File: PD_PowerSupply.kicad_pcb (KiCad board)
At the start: 2 copper layers, 10 parts, among them J1 USB4085-GF-A_REVA, Q1 STL6P3LLH6, Q2 STL6P3LLH6, U1 STUSB4500QTR, U2 ESP32-WROOM-32, U3 CP2102N, U4 IR38062MTRPBF, U5 IR38062MTRPBF, U6 LTC3886

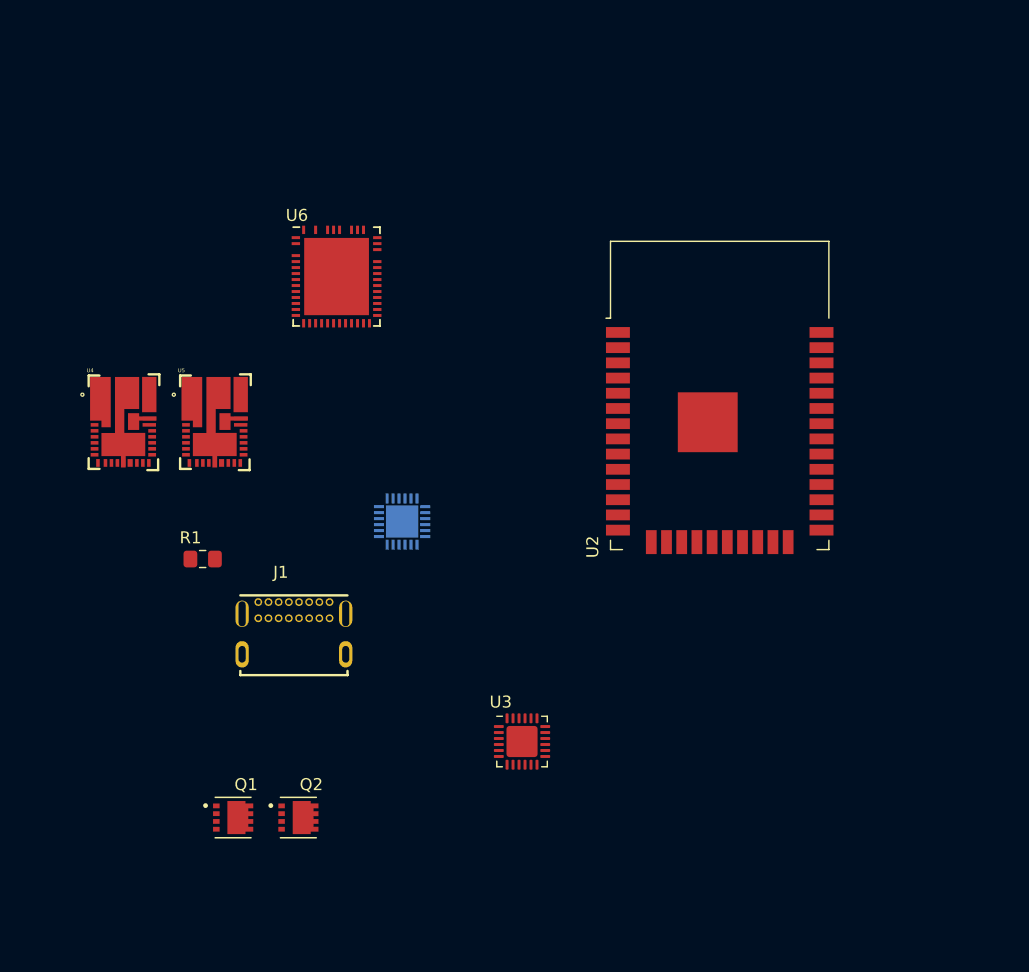
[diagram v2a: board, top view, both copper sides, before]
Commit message: added footprints and symbol for LTC2972
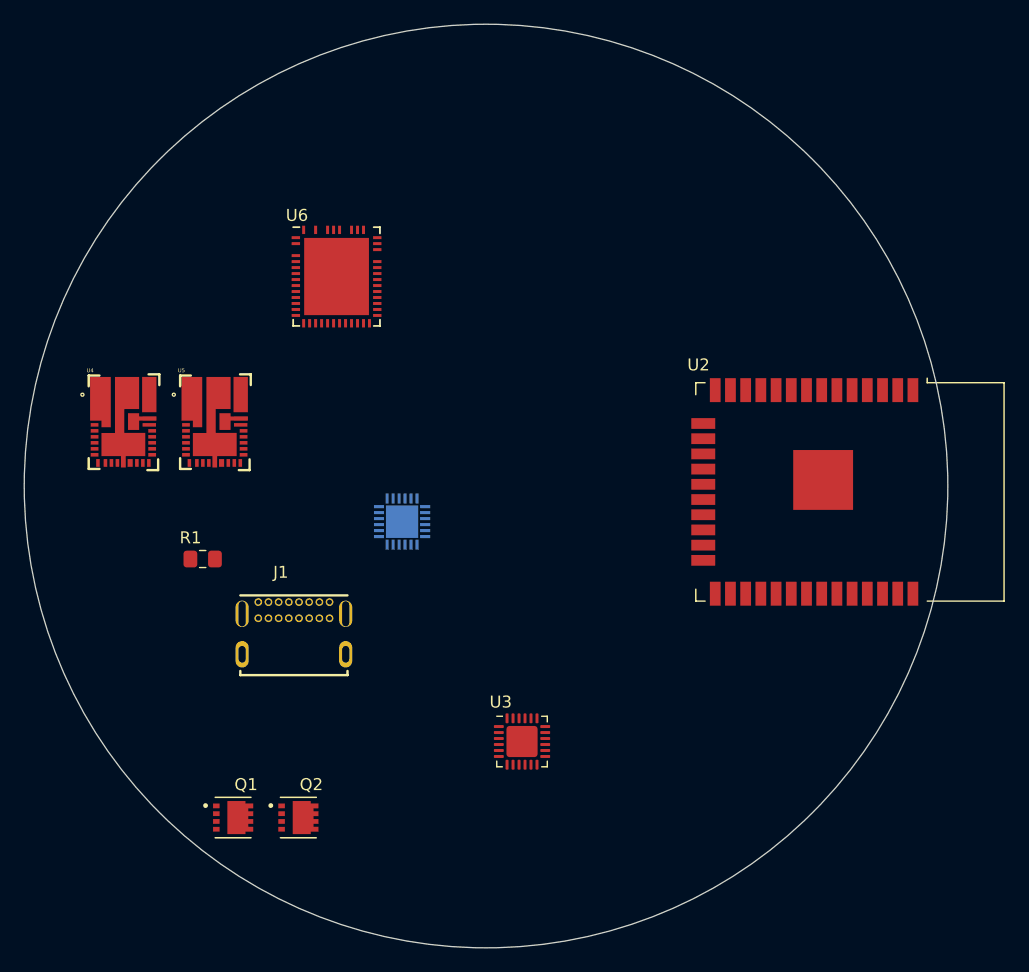
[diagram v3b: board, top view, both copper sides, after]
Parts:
- moved U2 9.37 mm to (110.8, 102.3), turned to 270 degrees
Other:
- board outline added: 77.1 x 77.1 mm
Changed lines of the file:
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@@
   (general
     (thickness 1.6)
-    (drawings 0)
+    (drawings 1)
     (tracks 0)
     (zones 0)
@@
   )
   (module RF_Module:ESP32-WROOM-32 (layer F.Cu)
-    (at 102.87 97.282)
+    (at 110.751 102.346 270)
     (descr "Single 2.4 GHz Wi-Fi and Bluetooth combo chip https://www.espressif.com/sites/default/files/documentation/esp32-wroom-32_datasheet_en.pdf")
     (tags "Single 2.4 GHz Wi-Fi and Bluetooth combo  chip")
     (attr smd)
-    (fp_text reference U2 (at -10.61 9.652 90) (layer F.SilkS)
+    (fp_text reference U2 (at -10.61 9.652) (layer F.SilkS)
       (effects (font (size 1 1) (thickness 0.15)))
     )
-    (fp_text value ESP32-WROOM-32 (at 0 11.5) (layer F.Fab)
+    (fp_text value ESP32-WROOM-32 (at 0 11.5 90) (layer F.Fab)
       (effects (font (size 1 1) (thickness 0.15)))
     )
@@
     (fp_line (start 9 9.76) (end 9 -15.745) (layer F.Fab) (width 0.1))
     (fp_line (start -14 -9.97) (end -14 -20.75) (layer Dwgs.User) (width 0.1))
-    (fp_text user "5 mm" (at 7.8 -19.075 90) (layer Cmts.User)
+    (fp_text user "5 mm" (at 7.8 -19.075) (layer Cmts.User)
       (effects (font (size 0.5 0.5) (thickness 0.1)))
     )
-    (fp_text user "5 mm" (at -11.2 -14.375) (layer Cmts.User)
+    (fp_text user "5 mm" (at -11.2 -14.375 90) (layer Cmts.User)
       (effects (font (size 0.5 0.5) (thickness 0.1)))
     )
-    (fp_text user "5 mm" (at 11.8 -14.375) (layer Cmts.User)
+    (fp_text user "5 mm" (at 11.8 -14.375 90) (layer Cmts.User)
       (effects (font (size 0.5 0.5) (thickness 0.1)))
     )
-    (fp_text user Antenna (at 0 -13) (layer Cmts.User)
+    (fp_text user Antenna (at 0 -13 90) (layer Cmts.User)
       (effects (font (size 1 1) (thickness 0.15)))
     )
-    (fp_text user "KEEP-OUT ZONE" (at 0 -19) (layer Cmts.User)
+    (fp_text user "KEEP-OUT ZONE" (at 0 -19 90) (layer Cmts.User)
       (effects (font (size 1 1) (thickness 0.15)))
     )
-    (fp_text user %R (at 0 0) (layer F.Fab)
+    (fp_text user %R (at 0 0 90) (layer F.Fab)
       (effects (font (size 1 1) (thickness 0.15)))
     )
-    (pad 38 smd rect (at 8.5 -8.255) (size 2 0.9) (layers F.Cu F.Paste F.Mask)
-      (net 42 GND))
-    (pad 37 smd rect (at 8.5 -6.985) (size 2 0.9) (layers F.Cu F.Paste F.Mask)
+    (pad 38 smd rect (at 8.5 -8.255 270) (size 2 0.9) (layers F.Cu F.Paste F.Mask)
+      (net 42 GND))
+    (pad 37 smd rect (at 8.5 -6.985 270) (size 2 0.9) (layers F.Cu F.Paste F.Mask)
       (net 1 "Net-(U2-Pad37)"))
-    (pad 36 smd rect (at 8.5 -5.715) (size 2 0.9) (layers F.Cu F.Paste F.Mask)
+    (pad 36 smd rect (at 8.5 -5.715 270) (size 2 0.9) (layers F.Cu F.Paste F.Mask)
       (net 2 /I2C_SCL))
-    (pad 35 smd rect (at 8.5 -4.445) (size 2 0.9) (layers F.Cu F.Paste F.Mask)
+    (pad 35 smd rect (at 8.5 -4.445 270) (size 2 0.9) (layers F.Cu F.Paste F.Mask)
       (net 3 "Net-(U2-Pad35)"))
-    (pad 34 smd rect (at 8.5 -3.175) (size 2 0.9) (layers F.Cu F.Paste F.Mask)
+    (pad 34 smd rect (at 8.5 -3.175 270) (size 2 0.9) (layers F.Cu F.Paste F.Mask)
       (net 4 "Net-(U2-Pad34)"))
-    (pad 33 smd rect (at 8.5 -1.905) (size 2 0.9) (layers F.Cu F.Paste F.Mask)
+    (pad 33 smd rect (at 8.5 -1.905 270) (size 2 0.9) (layers F.Cu F.Paste F.Mask)
       (net 5 /I2C_SDA))
-    (pad 32 smd rect (at 8.5 -0.635) (size 2 0.9) (layers F.Cu F.Paste F.Mask)
+    (pad 32 smd rect (at 8.5 -0.635 270) (size 2 0.9) (layers F.Cu F.Paste F.Mask)
       (net 6 "Net-(U2-Pad32)"))
-    (pad 31 smd rect (at 8.5 0.635) (size 2 0.9) (layers F.Cu F.Paste F.Mask)
+    (pad 31 smd rect (at 8.5 0.635 270) (size 2 0.9) (layers F.Cu F.Paste F.Mask)
       (net 7 "Net-(U2-Pad31)"))
-    (pad 30 smd rect (at 8.5 1.905) (size 2 0.9) (layers F.Cu F.Paste F.Mask)
+    (pad 30 smd rect (at 8.5 1.905 270) (size 2 0.9) (layers F.Cu F.Paste F.Mask)
       (net 8 "Net-(U2-Pad30)"))
-    (pad 29 smd rect (at 8.5 3.175) (size 2 0.9) (layers F.Cu F.Paste F.Mask)
+    (pad 29 smd rect (at 8.5 3.175 270) (size 2 0.9) (layers F.Cu F.Paste F.Mask)
       (net 9 "Net-(U2-Pad29)"))
-    (pad 28 smd rect (at 8.5 4.445) (size 2 0.9) (layers F.Cu F.Paste F.Mask)
+    (pad 28 smd rect (at 8.5 4.445 270) (size 2 0.9) (layers F.Cu F.Paste F.Mask)
       (net 10 "Net-(U2-Pad28)"))
-    (pad 27 smd rect (at 8.5 5.715) (size 2 0.9) (layers F.Cu F.Paste F.Mask)
+    (pad 27 smd rect (at 8.5 5.715 270) (size 2 0.9) (layers F.Cu F.Paste F.Mask)
       (net 11 "Net-(U2-Pad27)"))
-    (pad 26 smd rect (at 8.5 6.985) (size 2 0.9) (layers F.Cu F.Paste F.Mask)
+    (pad 26 smd rect (at 8.5 6.985 270) (size 2 0.9) (layers F.Cu F.Paste F.Mask)
       (net 12 "Net-(U2-Pad26)"))
-    (pad 25 smd rect (at 8.5 8.255) (size 2 0.9) (layers F.Cu F.Paste F.Mask)
+    (pad 25 smd rect (at 8.5 8.255 270) (size 2 0.9) (layers F.Cu F.Paste F.Mask)
       (net 13 "Net-(U2-Pad25)"))
-    (pad 24 smd rect (at 5.715 9.255 90) (size 2 0.9) (layers F.Cu F.Paste F.Mask)
+    (pad 24 smd rect (at 5.715 9.255) (size 2 0.9) (layers F.Cu F.Paste F.Mask)
       (net 14 "Net-(U2-Pad24)"))
-    (pad 23 smd rect (at 4.445 9.255 90) (size 2 0.9) (layers F.Cu F.Paste F.Mask)
+    (pad 23 smd rect (at 4.445 9.255) (size 2 0.9) (layers F.Cu F.Paste F.Mask)
       (net 15 "Net-(U2-Pad23)"))
-    (pad 22 smd rect (at 3.175 9.255 90) (size 2 0.9) (layers F.Cu F.Paste F.Mask)
+    (pad 22 smd rect (at 3.175 9.255) (size 2 0.9) (layers F.Cu F.Paste F.Mask)
       (net 16 "Net-(U2-Pad22)"))
-    (pad 21 smd rect (at 1.905 9.255 90) (size 2 0.9) (layers F.Cu F.Paste F.Mask)
+    (pad 21 smd rect (at 1.905 9.255) (size 2 0.9) (layers F.Cu F.Paste F.Mask)
       (net 17 "Net-(U2-Pad21)"))
-    (pad 20 smd rect (at 0.635 9.255 90) (size 2 0.9) (layers F.Cu F.Paste F.Mask)
+    (pad 20 smd rect (at 0.635 9.255) (size 2 0.9) (layers F.Cu F.Paste F.Mask)
       (net 18 "Net-(U2-Pad20)"))
-    (pad 19 smd rect (at -0.635 9.255 90) (size 2 0.9) (layers F.Cu F.Paste F.Mask)
+    (pad 19 smd rect (at -0.635 9.255) (size 2 0.9) (layers F.Cu F.Paste F.Mask)
       (net 19 "Net-(U2-Pad19)"))
-    (pad 18 smd rect (at -1.905 9.255 90) (size 2 0.9) (layers F.Cu F.Paste F.Mask)
+    (pad 18 smd rect (at -1.905 9.255) (size 2 0.9) (layers F.Cu F.Paste F.Mask)
       (net 20 "Net-(U2-Pad18)"))
-    (pad 17 smd rect (at -3.175 9.255 90) (size 2 0.9) (layers F.Cu F.Paste F.Mask)
+    (pad 17 smd rect (at -3.175 9.255) (size 2 0.9) (layers F.Cu F.Paste F.Mask)
       (net 21 "Net-(U2-Pad17)"))
-    (pad 16 smd rect (at -4.445 9.255 90) (size 2 0.9) (layers F.Cu F.Paste F.Mask)
+    (pad 16 smd rect (at -4.445 9.255) (size 2 0.9) (layers F.Cu F.Paste F.Mask)
       (net 22 "Net-(U2-Pad16)"))
-    (pad 15 smd rect (at -5.715 9.255 90) (size 2 0.9) (layers F.Cu F.Paste F.Mask)
-      (net 42 GND))
-    (pad 14 smd rect (at -8.5 8.255) (size 2 0.9) (layers F.Cu F.Paste F.Mask)
+    (pad 15 smd rect (at -5.715 9.255) (size 2 0.9) (layers F.Cu F.Paste F.Mask)
+      (net 42 GND))
+    (pad 14 smd rect (at -8.5 8.255 270) (size 2 0.9) (layers F.Cu F.Paste F.Mask)
       (net 23 "Net-(U2-Pad14)"))
-    (pad 13 smd rect (at -8.5 6.985) (size 2 0.9) (layers F.Cu F.Paste F.Mask)
+    (pad 13 smd rect (at -8.5 6.985 270) (size 2 0.9) (layers F.Cu F.Paste F.Mask)
       (net 24 "Net-(U2-Pad13)"))
-    (pad 12 smd rect (at -8.5 5.715) (size 2 0.9) (layers F.Cu F.Paste F.Mask)
+    (pad 12 smd rect (at -8.5 5.715 270) (size 2 0.9) (layers F.Cu F.Paste F.Mask)
       (net 25 "Net-(U2-Pad12)"))
-    (pad 11 smd rect (at -8.5 4.445) (size 2 0.9) (layers F.Cu F.Paste F.Mask)
+    (pad 11 smd rect (at -8.5 4.445 270) (size 2 0.9) (layers F.Cu F.Paste F.Mask)
       (net 26 "Net-(U2-Pad11)"))
-    (pad 10 smd rect (at -8.5 3.175) (size 2 0.9) (layers F.Cu F.Paste F.Mask)
+    (pad 10 smd rect (at -8.5 3.175 270) (size 2 0.9) (layers F.Cu F.Paste F.Mask)
       (net 27 "Net-(U2-Pad10)"))
-    (pad 9 smd rect (at -8.5 1.905) (size 2 0.9) (layers F.Cu F.Paste F.Mask)
+    (pad 9 smd rect (at -8.5 1.905 270) (size 2 0.9) (layers F.Cu F.Paste F.Mask)
       (net 28 "Net-(U2-Pad9)"))
-    (pad 8 smd rect (at -8.5 0.635) (size 2 0.9) (layers F.Cu F.Paste F.Mask)
+    (pad 8 smd rect (at -8.5 0.635 270) (size 2 0.9) (layers F.Cu F.Paste F.Mask)
       (net 29 "Net-(U2-Pad8)"))
-    (pad 7 smd rect (at -8.5 -0.635) (size 2 0.9) (layers F.Cu F.Paste F.Mask)
+    (pad 7 smd rect (at -8.5 -0.635 270) (size 2 0.9) (layers F.Cu F.Paste F.Mask)
       (net 53 /STUSB_ALERT))
-    (pad 6 smd rect (at -8.5 -1.905) (size 2 0.9) (layers F.Cu F.Paste F.Mask)
+    (pad 6 smd rect (at -8.5 -1.905 270) (size 2 0.9) (layers F.Cu F.Paste F.Mask)
       (net 50 /STUSB_RESET))
-    (pad 5 smd rect (at -8.5 -3.175) (size 2 0.9) (layers F.Cu F.Paste F.Mask)
+    (pad 5 smd rect (at -8.5 -3.175 270) (size 2 0.9) (layers F.Cu F.Paste F.Mask)
       (net 30 "Net-(U2-Pad5)"))
-    (pad 4 smd rect (at -8.5 -4.445) (size 2 0.9) (layers F.Cu F.Paste F.Mask)
+    (pad 4 smd rect (at -8.5 -4.445 270) (size 2 0.9) (layers F.Cu F.Paste F.Mask)
       (net 31 "Net-(U2-Pad4)"))
-    (pad 3 smd rect (at -8.5 -5.715) (size 2 0.9) (layers F.Cu F.Paste F.Mask)
+    (pad 3 smd rect (at -8.5 -5.715 270) (size 2 0.9) (layers F.Cu F.Paste F.Mask)
       (net 32 "Net-(U2-Pad3)"))
-    (pad 2 smd rect (at -8.5 -6.985) (size 2 0.9) (layers F.Cu F.Paste F.Mask)
+    (pad 2 smd rect (at -8.5 -6.985 270) (size 2 0.9) (layers F.Cu F.Paste F.Mask)
       (net 59 +3V3))
-    (pad 1 smd rect (at -8.5 -8.255) (size 2 0.9) (layers F.Cu F.Paste F.Mask)
-      (net 42 GND))
-    (pad 39 smd rect (at -1 -0.755) (size 5 5) (layers F.Cu F.Paste F.Mask)
+    (pad 1 smd rect (at -8.5 -8.255 270) (size 2 0.9) (layers F.Cu F.Paste F.Mask)
+      (net 42 GND))
+    (pad 39 smd rect (at -1 -0.755 270) (size 5 5) (layers F.Cu F.Paste F.Mask)
       (net 42 GND))
     (model ${KISYS3DMOD}/RF_Module.3dshapes/ESP32-WROOM-32.wrl
@@
     )
   )
+  (gr_circle (center 83.354636 101.854) (end 120.692636 111.506) (layer Edge.Cuts) (width 0.05))
 )

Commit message: set up coprocessor
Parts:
- added Q3: MMBT3906, Package_TO_SOT_SMD:SOT-23, F.Cu at (94.1, 132.8)
- added Q4: MMBT3906, Package_TO_SOT_SMD:SOT-23, F.Cu at (98.5, 132.8)
- U4, U5: value IR38062MTRPBF -> LTM8074IY#PBF; footprint IR38062MTRPBF:PQFN50P700X500X100-26N -> LTM8074IY_PBF:BGA25C65P5X5_400X400X198N
- U6: value LTC3886 -> LTC2972; footprint Package_DFN_QFN:Linear_UGK52_QFN-46-52 -> LTC2972:LTC2972
- moved U4 53.1 mm to (98.4, 124.1)
- moved U5 52.6 mm to (107.2, 121.2)
- moved U6 37.3 mm to (94.0, 113.6)
- renumbered J1 to USB1
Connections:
- Q1 pad 5_6_7_8: VBUS -> Net-(D1-Pad2)
- U6 pad 19: Net-(U6-Pad19) -> GND
- U6 pad 2: Net-(U6-Pad2) -> GND
- U6 pad 25: Net-(U6-Pad25) -> +3V3
- U6 pad 26: Net-(U6-Pad26) -> GND
- U6 pad 27: Net-(U6-Pad27) -> GND
- U6 pad 33: Net-(U6-Pad33) -> GND
- U6 pad 4: Net-(U6-Pad4) -> /vSINK
- U6 pad 40: Net-(U6-Pad40) -> Net-(U5-PadA2)
- U6 pad 5: Net-(U6-Pad5) -> /vSINK
- U6 pad 6: Net-(U6-Pad6) -> Net-(C11-Pad2)
- U6 pad 7: Net-(U6-Pad7) -> Net-(C11-Pad2)
- U6 pad 8: Net-(U6-Pad8) -> Net-(C10-Pad2)
- U6 pad 9: Net-(U6-Pad9) -> Net-(C10-Pad2)
- USB1 pad A4: VBUS -> Net-(D1-Pad2)
- USB1 pad A9: VBUS -> Net-(D1-Pad2)
- USB1 pad B4: VBUS -> Net-(D1-Pad2)
- USB1 pad B9: VBUS -> Net-(D1-Pad2)
